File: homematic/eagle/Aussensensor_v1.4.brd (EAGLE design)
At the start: 56.2 x 29.4 mm, 41 parts, among them IC1 Atmega 328P, IC2 MAX1724, IC3 TSL2561, IC4 BMP180, IC5 BME280, IC6 DS18B20, T1 IRML6344

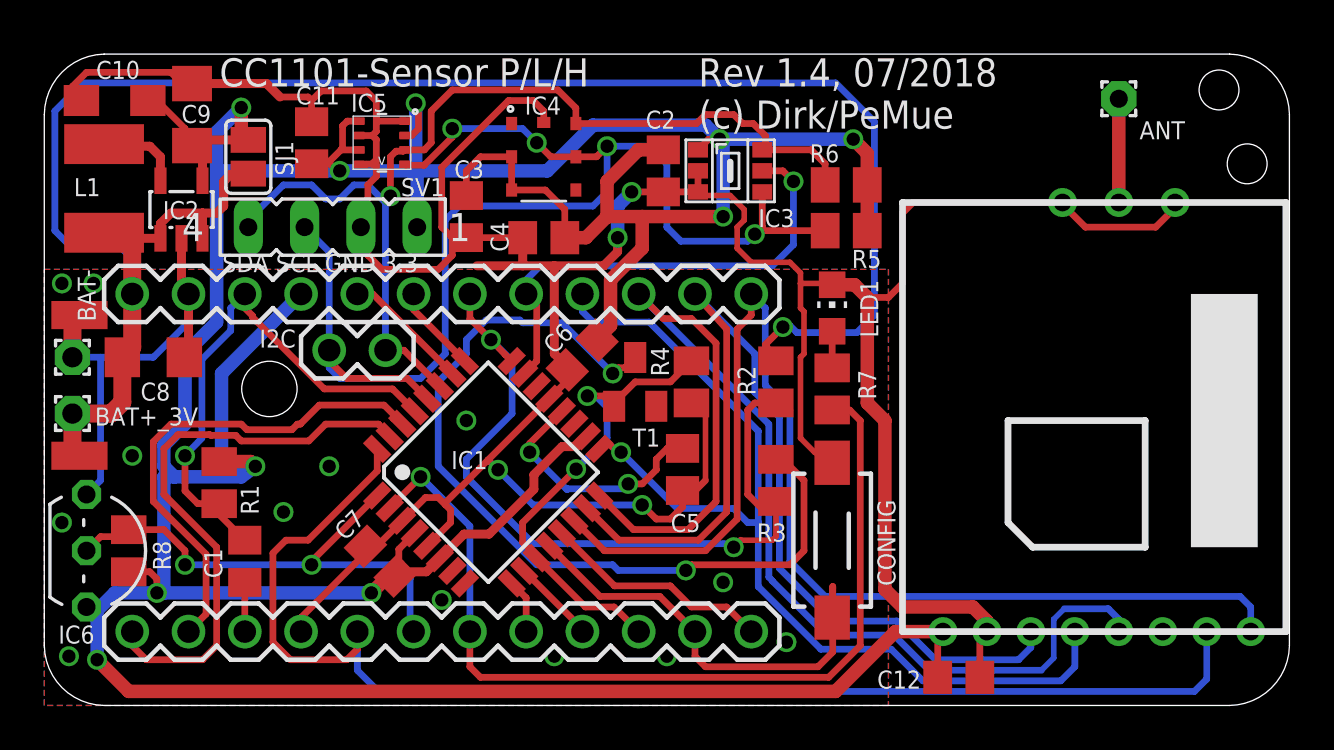
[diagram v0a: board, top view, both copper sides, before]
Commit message: added SJ2 for battery voltage measurement w/o battery load
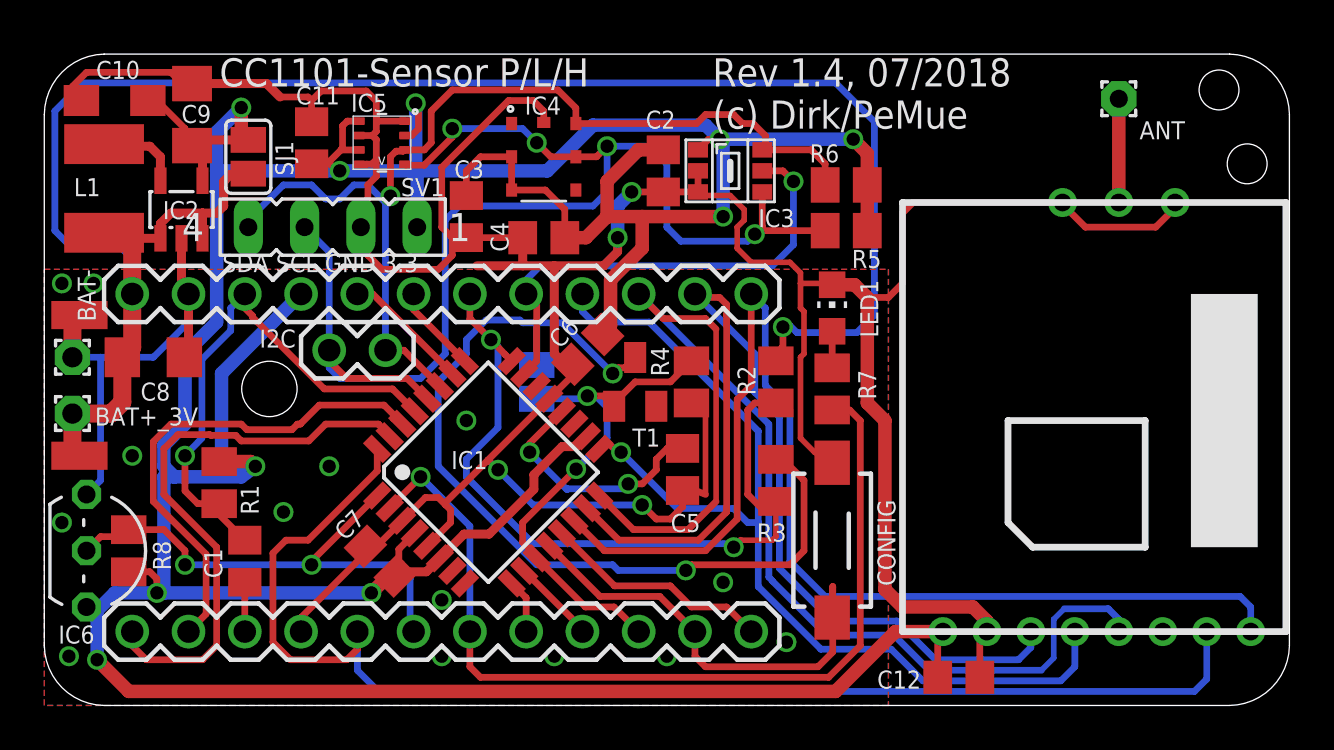
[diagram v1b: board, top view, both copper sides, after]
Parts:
- added SJ2: (no value), jumper:SJ
- moved C6 0.36 mm to (24.5, 16.1)
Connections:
- net D7: now also SJ2.2
- net N$3: now also SJ2.1
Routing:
- net D7: track 21.6 -> 24.0 mm
- net N$3: track 39.2 -> 41.1 mm
- net MOSI: track 45.8 -> 46.4 mm
- net GND: track 186.7 -> 187.2 mm, vias 17 -> 18
- net A1: track 35.2 -> 34.6 mm

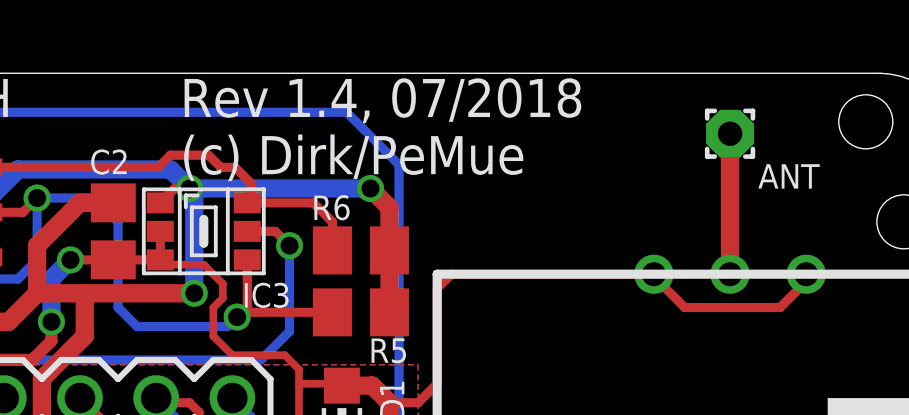
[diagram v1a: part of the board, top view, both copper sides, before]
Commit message: replaced 10k by 4k7 for DS18x20 in Aussensensor v1.4 and v1.5
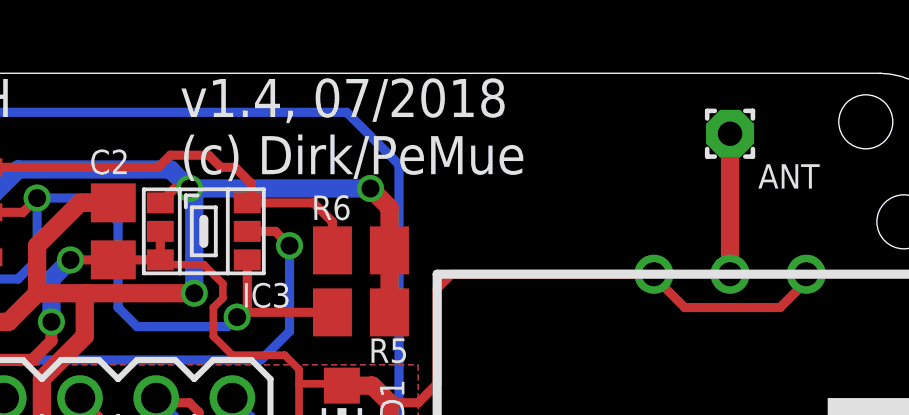
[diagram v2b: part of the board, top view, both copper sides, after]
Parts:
- R8: value 10k -> 4k7
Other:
- board text added: "v1.4, 07/2018 (c) Dirk/PeMue"
- board text removed: "Rev 1.4, 07/2018 (c) Dirk/PeMue"
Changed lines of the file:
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@@
 <plain>
 <text x="7.9058" y="27.94" size="1.27" layer="25">CC1101-Sensor P/L/H</text>
-<text x="30.16255" y="26.03505" size="1.27" layer="25">Rev 1.4, 07/2018
+<text x="30.16255" y="26.03505" size="1.27" layer="25">v1.4, 07/2018
 (c) Dirk/PeMue</text>
 <wire x1="2.69875" y1="29.4" x2="53.49875" y2="29.4" width="0" layer="20"/>
@@
 <attribute name="VALUE" x="-1.397" y="9.525" size="1.27" layer="27" ratio="10" rot="R270"/>
 </element>
-<element name="R8" library="rcl" package="M0805" value="10k" x="3.81" y="6.985" smashed="yes" rot="R90">
+<element name="R8" library="rcl" package="M0805" value="4k7" x="3.81" y="6.985" smashed="yes" rot="R90">
 <attribute name="NAME" x="5.715" y="6.096" size="0.8128" layer="25" rot="R90"/>
 <attribute name="VALUE" x="6.096" y="5.969" size="1.27" layer="27" rot="R90"/>
